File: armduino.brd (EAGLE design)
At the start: 68.6 x 53.4 mm, 63 parts, among them IC1 7805DT, IC2 LM358D, IC3 LM1117-3.3V, Q1 FDN360P, Q2 20MHz, Q3 8MHz, U2 MKE02Z64VLD4, U3 MKL26ZVFM4, X1 POWERSUPPLY_DC21MMX, X2 USB-B_TH

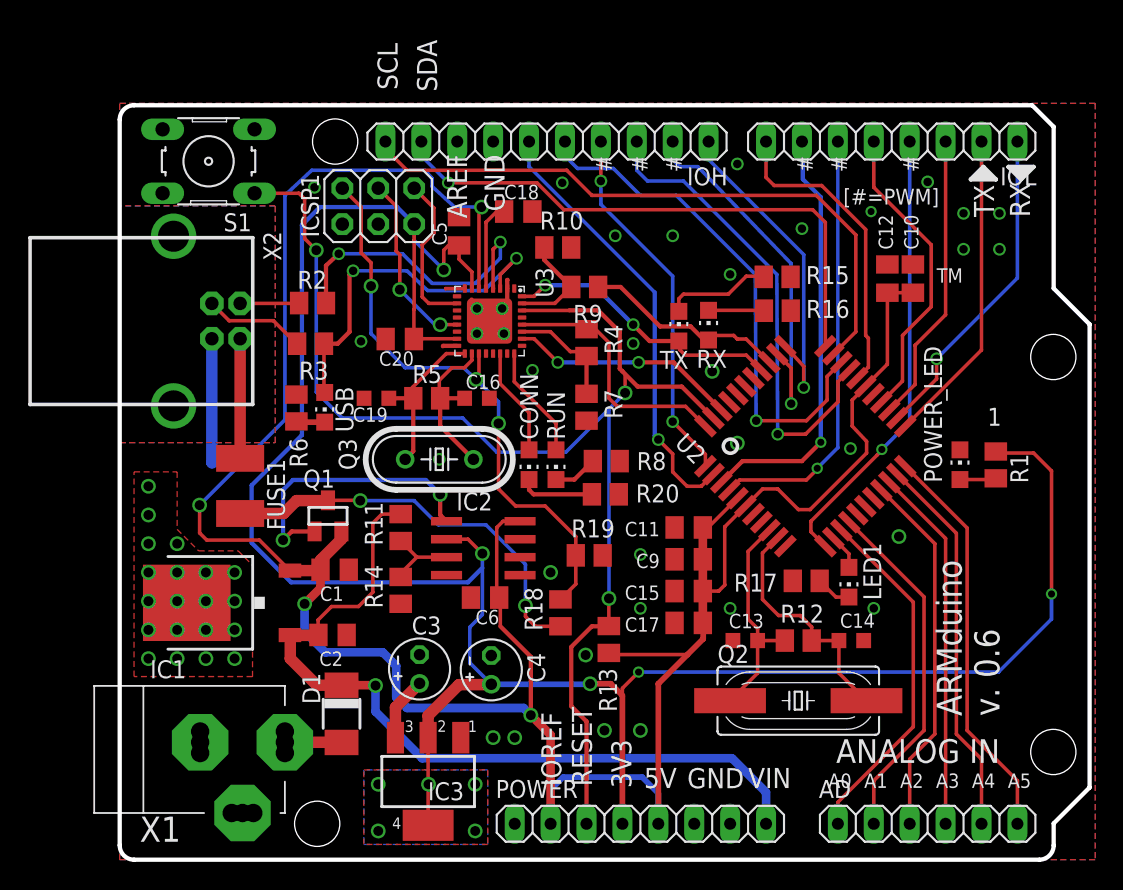
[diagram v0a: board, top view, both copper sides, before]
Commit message: Modifications to v0.7:  * Schematic parts grouped together;  * KL26 footprint edited with extended pads, for easier soldering;  * SWD signal rerouting to avoid transpositions and unnecessary curves;  * Added SWD connection for external target;  * Corrected Programmer name.
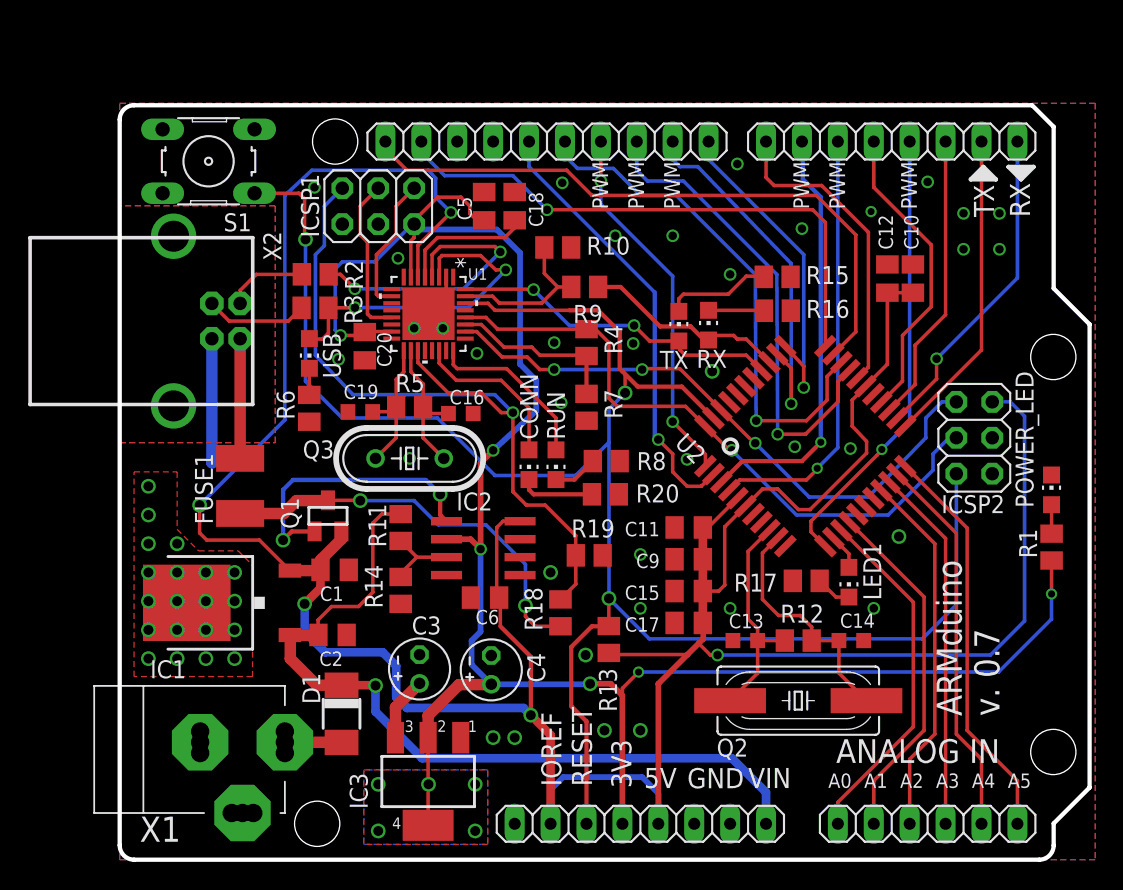
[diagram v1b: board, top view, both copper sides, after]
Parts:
- removed U3: MKL26ZVFM4, freescale:QFN32
- added ICSP2: 3x2 M, SmartPrj:2X03
- added U1: MKL26Z128VFM4, freescale:QFN-32_5X5X0.9
- moved R1 7.03 mm to (65.9, 22.1), turned to 270 degrees
- moved POWER_LED 6.72 mm to (65.9, 26.2)
- moved USB 3.96 mm to (13.4, 35.8)
- moved R3 2.56 mm to (13.8, 39.0)
- moved C20 2.53 mm to (17.3, 36.3), turned to 270 degrees
- moved C5 2.51 mm to (25.8, 46.2)
- moved Q3 2.10 mm to (20.5, 28.4)
- moved R2 2.04 mm to (13.8, 41.4)
- moved C16 1.57 mm to (24.1, 31.6)
- moved C19 1.49 mm to (17.0, 31.7)
- moved R5 1.36 mm to (20.5, 32.0)
- moved R6 0.91 mm to (13.4, 31.9), turned to 270 degrees
- moved C18 0.46 mm to (27.9, 46.2), turned to 90 degrees
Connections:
- removed net N$14: CONN.A, U3.22
- removed net N$31: C18.1, U3.5
- new net N$10: C18.1, U1.5
- new net N$12: RUN.A, U1.24
- net +3V3: now also U1.15, U1.7; no longer U3.15, U3.7
- net +5V: now also ICSP2.2, U1.6; no longer U3.6
- net DEBUG_RESET: now also U1.19; no longer U3.19
- net DEBUG_SWCLK: now also U1.10; no longer U3.10
- net DEBUG_SWDIO: now also U1.13; no longer U3.13
- net GND: now also ICSP2.6, U1.16, U1.2, U1.33, U1.8; no longer U3.16, U3.2, U3.8, U3.EXP
- net N$13: now also CONN.A, U1.22; no longer RUN.A, U3.24
- net N$24: now also U1.17; no longer U3.17
- net N$25: now also U1.18; no longer U3.18
- net N$6: now also U1.31; no longer U3.31
- net N$8: now also U1.27; no longer U3.27
- net PROG_NRESET: now also ICSP2.5, U1.30; no longer U3.30
- net PROG_SWCLK: now also ICSP2.1, U1.26; no longer U3.26
- net PROG_SWDIO: now also ICSP2.3, U1.28; no longer U3.28
- net PROG_TX: now also U1.32; no longer U3.32
- net USB_D+: now also U1.3; no longer U3.3
- net USB_D-: now also U1.4; no longer U3.4
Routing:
- net PROG_NRESET: track 94.5 -> 135.1 mm
- net +5V: track 188.4 -> 228.1 mm, vias 4 -> 5
- net PROG_SWDIO: track 18.2 -> 46.2 mm, vias 0 -> 1
- net PROG_SWCLK: track 16.2 -> 43.3 mm, vias 2 -> 3
- net +3V3: track 165.1 -> 139.8 mm, vias 10 -> 11
- net N$12: track 0.00 -> 12.1 mm
- net DEBUG_RESET: track 41.9 -> 53.6 mm, vias 3 -> 1
- net N$10: track 0.00 -> 9.44 mm
- net N$14: track 7.66 -> 0.00 mm
- net N$31: track 6.28 -> 0.00 mm
- net N$8: track 7.94 -> 12.2 mm
- net N$6: track 7.55 -> 11.4 mm
- net PROG_TX: track 20.1 -> 23.6 mm
- net N$13: track 8.03 -> 11.5 mm
- net USB_D+: track 25.7 -> 23.5 mm
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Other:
- board text added: "ARMduino v. 0.7"
- board text added: "PWM"
- board text added: "U1"
- board text removed: "#"
- board text removed: "1"
- board text removed: "AREF"
- board text removed: "ARMduino v. 0.6"
- board text removed: "SCL"
- board text removed: "SDA"
- board text removed: "TM"
- board text removed: "[#=PWM]"

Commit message: Add led values according to colors to be used and fuse value.
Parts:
- CONN, RUN, RX, TX, USB: value (none) -> YELLOW
- FUSE1: value (none) -> Reseteable - 500mA
- LED1: value (none) -> BLUE
- POWER_LED: value (none) -> GREEN
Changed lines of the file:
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@@
 <attribute name="VALUE" x="13.1375" y="12.958" size="1.27" layer="27" ratio="10" rot="R270"/>
 </element>
-<element name="POWER_LED" library="led" package="CHIP-LED0805" value="" x="65.913" y="26.162"/>
+<element name="POWER_LED" library="led" package="CHIP-LED0805" value="GREEN" x="65.913" y="26.162"/>
 <element name="R1" library="rcl" package="M0805" value="120r" x="65.919" y="22.1135" smashed="yes" rot="R270">
 <attribute name="NAME" x="64.891" y="21.3205" size="1.27" layer="25" rot="R90"/>
 <attribute name="VALUE" x="63.379" y="23.3835" size="1.27" layer="27" rot="R270"/>
 </element>
-<element name="FUSE1" library="rcl" package="L1812" value="" x="8.52" y="26.4395" smashed="yes" rot="R270">
+<element name="FUSE1" library="rcl" package="L1812" value="Reseteable - 500mA" x="8.52" y="26.4395" smashed="yes" rot="R270">
 <attribute name="NAME" x="6.593" y="23.7255" size="1.27" layer="25" rot="R90"/>
 <attribute name="VALUE" x="5.345" y="28.3445" size="1.27" layer="27" rot="R270"/>
@@
 <attribute name="VALUE" x="15.0875" y="41.58" size="1.27" layer="27" rot="R180"/>
 </element>
-<element name="USB" library="led" package="CHIP-LED0805" value="" x="13.4205" y="35.81" smashed="yes" rot="R180">
+<element name="USB" library="led" package="CHIP-LED0805" value="YELLOW" x="13.4205" y="35.81" smashed="yes" rot="R180">
 <attribute name="NAME" x="14.373" y="37.2705" size="1.27" layer="25" rot="R270"/>
 <attribute name="VALUE" x="10.8805" y="37.08" size="1.27" layer="27" rot="R270"/>
@@
 <attribute name="VALUE" x="41.25" y="18.65" size="1.016" layer="27" rot="R180"/>
 </element>
-<element name="TX" library="led" package="CHIP-LED0805" value="" x="39.551" y="37.738" smashed="yes">
+<element name="TX" library="led" package="CHIP-LED0805" value="YELLOW" x="39.551" y="37.738" smashed="yes">
 <attribute name="NAME" x="40.24" y="35.995" size="1.27" layer="25" rot="R180"/>
 <attribute name="VALUE" x="42.091" y="36.468" size="1.27" layer="27" rot="R90"/>
@@
 <attribute name="VALUE" x="45.237" y="38.688" size="1.27" layer="27"/>
 </element>
-<element name="RX" library="led" package="CHIP-LED0805" value="" x="41.652" y="37.81" smashed="yes">
+<element name="RX" library="led" package="CHIP-LED0805" value="YELLOW" x="41.652" y="37.81" smashed="yes">
 <attribute name="NAME" x="42.962" y="36.064" size="1.27" layer="25" rot="R180"/>
 <attribute name="VALUE" x="44.192" y="36.54" size="1.27" layer="27" rot="R90"/>
@@
 <attribute name="VALUE" x="45.249" y="36.294" size="1.27" layer="27"/>
 </element>
-<element name="LED1" library="led" package="CHIP-LED0805" value="" x="51.583" y="19.627" smashed="yes" rot="R180">
+<element name="LED1" library="led" package="CHIP-LED0805" value="BLUE" x="51.583" y="19.627" smashed="yes" rot="R180">
 <attribute name="NAME" x="52.599" y="22.421" size="1.27" layer="25" rot="R270"/>
 <attribute name="VALUE" x="49.043" y="20.897" size="1.27" layer="27" rot="R270"/>
@@
 <element name="R4" library="rcl" package="M0805" value="10k" x="33.02" y="36.576" rot="R270"/>
 <element name="R7" library="rcl" package="M0805" value="20k" x="33.02" y="32.004" rot="R270"/>
-<element name="RUN" library="led" package="CHIP-LED0805" value="" x="30.861" y="27.94" smashed="yes" rot="R180">
+<element name="RUN" library="led" package="CHIP-LED0805" value="YELLOW" x="30.861" y="27.94" smashed="yes" rot="R180">
 <attribute name="NAME" x="31.496" y="29.718" size="1.27" layer="25" rot="R90"/>
 <attribute name="VALUE" x="28.321" y="29.21" size="1.27" layer="27" rot="R270"/>
 </element>
-<element name="CONN" library="led" package="CHIP-LED0805" value="" x="28.956" y="27.94" smashed="yes" rot="R180">
+<element name="CONN" library="led" package="CHIP-LED0805" value="YELLOW" x="28.956" y="27.94" smashed="yes" rot="R180">
 <attribute name="NAME" x="29.591" y="29.718" size="1.27" layer="25" rot="R90"/>
 <attribute name="VALUE" x="26.416" y="29.21" size="1.27" layer="27" rot="R270"/>

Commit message: Fixed target XTAL value, heat dissipation mask, update to version 0.7
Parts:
- Q2: value 20MHz -> 5MHz
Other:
- board text added: "ARMduino v. 0.8"
- board text removed: "ARMduino v. 0.7"
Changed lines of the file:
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@@
 <layer number="28" name="bValues" color="7" fill="1" visible="no" active="yes"/>
 <layer number="29" name="tStop" color="7" fill="3" visible="no" active="yes"/>
-<layer number="30" name="bStop" color="7" fill="6" visible="no" active="yes"/>
+<layer number="30" name="bStop" color="7" fill="6" visible="yes" active="yes"/>
 <layer number="31" name="tCream" color="7" fill="4" visible="no" active="yes"/>
 <layer number="32" name="bCream" color="7" fill="5" visible="no" active="yes"/>
@@
 <hole x="13.97" y="2.54" drill="3.2004"/>
 <text x="62.23" y="10.16" size="1.778" layer="21" rot="R90">ARMduino
-v. 0.7</text>
+v. 0.8</text>
 <wire x1="60.201" y1="48.121" x2="61.979" y2="48.121" width="0.3048" layer="21"/>
 <wire x1="61.979" y1="48.121" x2="61.09" y2="49.01" width="0.3048" layer="21"/>
@@
 </polygon>
 <polygon width="0.254" layer="29">
-<vertex x="1.016" y="23.368"/>
+<vertex x="1.016" y="27.94"/>
 <vertex x="1.016" y="13.208"/>
 <vertex x="10.16" y="13.208"/>
@@
 <vertex x="9.144" y="21.844"/>
 <vertex x="6.096" y="21.844"/>
-<vertex x="4.572" y="23.368"/>
+<vertex x="3.302" y="24.638"/>
+<vertex x="3.302" y="27.94"/>
 </polygon>
 <polygon width="0.254" layer="30">
@@
 <vertex x="6.096" y="21.844"/>
 <vertex x="4.572" y="23.368"/>
-<vertex x="4.572" y="29.464"/>
-<vertex x="1.016" y="29.464"/>
+<vertex x="4.572" y="28.575"/>
+<vertex x="1.016" y="28.575"/>
 </polygon>
 <text x="51.311" y="49.391" size="1.1176" layer="21" font="vector" ratio="13" rot="R90" align="bottom-right">PWM</text>
@@
 <attribute name="VALUE" x="22.098" y="50.673" size="1.27" layer="27" rot="R180"/>
 </element>
-<element name="Q2" library="crystal" package="SM49" value="20MHz" x="48" y="11.25" smashed="yes">
+<element name="Q2" library="crystal" package="SM49" value="5MHz" x="48" y="11.25" smashed="yes">
 <attribute name="MPN" value="" x="48" y="11.25" size="1.778" layer="27" display="off"/>
 <attribute name="MF" value="" x="48" y="11.25" size="1.778" layer="27" display="off"/>

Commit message: Fixed 100nF caps to same value.
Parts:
- C11, C15, C6: value 100nF/50V -> 100nF/25V
- C12: value 100nF/50v -> 100nF/25V
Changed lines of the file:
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@@
 <attribute name="VALUE" x="58.007" y="40.105" size="1.016" layer="27" rot="R90"/>
 </element>
-<element name="C11" library="rcl" package="C0805K" value="100nF/50V" x="40.25" y="23.5" smashed="yes" rot="R180">
+<element name="C11" library="rcl" package="C0805K" value="100nF/25V" x="40.25" y="23.5" smashed="yes" rot="R180">
 <attribute name="NAME" x="38.202" y="23.895" size="1.016" layer="25" rot="R180"/>
 <attribute name="VALUE" x="41.25" y="25.4" size="1.016" layer="27" rot="R180"/>
 </element>
-<element name="C12" library="rcl" package="C0805K" value="100nF/50v" x="54.3015" y="41.105" smashed="yes" rot="R90">
+<element name="C12" library="rcl" package="C0805K" value="100nF/25V" x="54.3015" y="41.105" smashed="yes" rot="R90">
 <attribute name="NAME" x="54.6965" y="43.153" size="1.016" layer="25" rot="R90"/>
 <attribute name="VALUE" x="56.2015" y="40.105" size="1.016" layer="27" rot="R90"/>
@@
 <attribute name="VALUE" x="50.95" y="13.85" size="1.016" layer="27"/>
 </element>
-<element name="C15" library="rcl" package="C0805K" value="100nF/50V" x="40.25" y="19" smashed="yes" rot="R180">
+<element name="C15" library="rcl" package="C0805K" value="100nF/25V" x="40.25" y="19" smashed="yes" rot="R180">
 <attribute name="NAME" x="38.202" y="19.395" size="1.016" layer="25" rot="R180"/>
 <attribute name="VALUE" x="41.25" y="20.9" size="1.016" layer="27" rot="R180"/>
@@
 <attribute name="VALUE" x="12.982" y="21.0705" size="1.27" layer="27"/>
 </element>
-<element name="C6" library="rcl" package="C0805K" value="100nF/50V" x="25.8445" y="18.542" rot="R180"/>
+<element name="C6" library="rcl" package="C0805K" value="100nF/25V" x="25.8445" y="18.542" rot="R180"/>
 <element name="S1" library="switch-omron" package="B3F-10XX" value="" x="6.2865" y="49.403" rot="R180">
 <attribute name="MF" value="" x="6.2865" y="49.403" size="1.778" layer="27" rot="R180" display="off"/>
